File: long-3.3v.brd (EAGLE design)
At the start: 43.8 x 50.2 mm, 20 parts, among them U1 USD-SOCKET, U2 MCP73831, U4 ADXL375BCCZ, X1 Micro USB

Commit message: Added RFM69HW and more stuff
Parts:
- added U$3: RFM69HW, RFM69HW:RFM69HW
- JP1, JP2, JP5, JP6: device pinhead:1X04 -> pinhead:1X02
- moved U$1 7.51 mm to (6.40, 8.30)
- moved JP2 7.50 mm to (18.4, 13.2)
- moved JP1 7.40 mm to (1.70, 13.2)
- moved U1 2.30 mm to (3.00, 34.5)
- moved JP4 0.60 mm to (18.7, 40.2)
- moved JP3 0.50 mm to (1.30, 40.3)
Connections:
- new net N$1: U$1.P$24, U$1.P$36, U$1.P$48
- new net N$2: U$1.P$23, U$1.P$35, U$1.P$47, U$1.P$49
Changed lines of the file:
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@@
 </autorouter>
 <elements>
-<element name="U1" library="SparkFun-Connectors" package="MICROSD_1:1" value="USD-SOCKET" x="3" y="32.2">
-<attribute name="PROD_ID" value="CONN-07820" x="3" y="32.2" size="1.778" layer="27" display="off"/>
+<element name="U1" library="SparkFun-Connectors" package="MICROSD_1:1" value="USD-SOCKET" x="3" y="34.5">
+<attribute name="PROD_ID" value="CONN-07820" x="3" y="34.5" size="1.778" layer="27" display="off"/>
 </element>
 <element name="D11" library="SparkFun" package="LED-0603" value="RED" x="1.4" y="7.4" rot="MR180"/>
@@
 <element name="X1" library="SparkFun" package="USB-MICROB" value="Micro USB" x="10" y="1.5"/>
 <element name="U$2" library="Ava" package="UBLOX_MAX" value="UBLOX_MAX" x="33.3" y="26.5"/>
-<element name="JP1" library="pinhead" package="1X04" value="" x="1.7" y="20.6" rot="MR90"/>
-<element name="JP2" library="pinhead" package="1X04" value="" x="18.4" y="20.7" rot="MR90"/>
-<element name="JP3" library="pinhead" package="1X04" value="" x="1.3" y="39.8" rot="MR90"/>
-<element name="JP4" library="pinhead" package="1X04" value="" x="18.7" y="39.6" rot="MR90"/>
-<element name="JP5" library="pinhead" package="1X04" value="" x="25.5" y="20.7" rot="MR90"/>
-<element name="JP6" library="pinhead" package="1X04" value="" x="42.2" y="20.7" rot="MR90"/>
+<element name="JP1" library="pinhead" package="1X02" value="" x="1.7" y="13.2" rot="MR90"/>
+<element name="JP2" library="pinhead" package="1X02" value="" x="18.4" y="13.2" rot="MR90"/>
+<element name="JP3" library="pinhead" package="1X04" value="" x="1.3" y="40.3" rot="MR90"/>
+<element name="JP4" library="pinhead" package="1X04" value="" x="18.7" y="40.2" rot="MR90"/>
+<element name="JP5" library="pinhead" package="1X02" value="" x="25.5" y="20.7" rot="MR90"/>
+<element name="JP6" library="pinhead" package="1X02" value="" x="42.2" y="20.7" rot="MR90"/>
 <element name="JP8" library="pinhead" package="1X04" value="" x="25.2" y="39.5" rot="MR90"/>
 <element name="JP9" library="pinhead" package="1X04" value="" x="42.4" y="39.6" rot="MR90"/>
 <element name="U4" library="adxl375bccz" package="LGA_CC-14-1" value="ADXL375BCCZ" x="33.4" y="42.1"/>
-<element name="U$1" library="STM32F411CEU6" package="STM32F411CEU6" value="STM32F411CEU6" x="6.7" y="15.8"/>
+<element name="U$1" library="STM32F411CEU6" package="STM32F411CEU6" value="STM32F411CEU6" x="6.4" y="8.3"/>
+<element name="U$3" library="RFM69HW" package="RFM69HW" value="RFM69HW" x="9.8" y="25.5" rot="R180"/>
 </elements>
 <signals>
@@
 <wire x1="10.25" y1="5.65" x2="11" y2="4.9" width="0.2" layer="16"/>
 <wire x1="11" y1="4.9" x2="11" y2="2.8" width="0.2" layer="16"/>
-<wire x1="11" y1="4.9" x2="11.3" y2="4.15" width="0" layer="19" extent="1-16"/>
 <wire x1="3" y1="6.85" x2="3.5" y2="6.85" width="0.2" layer="16"/>
 <wire x1="3.5" y1="6.85" x2="4.7" y2="5.65" width="0.2" layer="16"/>
@@
 <wire x1="3" y1="6.85" x2="2.4" y2="6.25" width="0.2" layer="16"/>
 <wire x1="2.4" y1="6.25" x2="2.4" y2="5.3001" width="0.2" layer="16"/>
+<wire x1="11" y1="4.9" x2="11.3" y2="4.15" width="0" layer="19" extent="1-16"/>
 </signal>
 <signal name="VBAT">
@@
 <contactref element="U$2" pad="1_GND"/>
 </signal>
+<signal name="N$1">
+<contactref element="U$1" pad="P$24"/>
+<contactref element="U$1" pad="P$48"/>
+<contactref element="U$1" pad="P$36"/>
+<wire x1="12.65" y1="8.525" x2="13.175" y2="14.55" width="0" layer="19" extent="1-1"/>
+<wire x1="7.15" y1="15.075" x2="13.175" y2="14.55" width="0" layer="19" extent="1-1"/>
+</signal>
+<signal name="N$2">
+<contactref element="U$1" pad="P$23"/>
+<contactref element="U$1" pad="P$35"/>
+<contactref element="U$1" pad="P$47"/>
+<contactref element="U$1" pad="P$49"/>
+<wire x1="9.9" y1="11.8" x2="13.175" y2="14.05" width="0" layer="19" extent="1-1"/>
+<wire x1="7.65" y1="15.075" x2="9.9" y2="11.8" width="0" layer="19" extent="1-1"/>
+<wire x1="12.15" y1="8.525" x2="9.9" y2="11.8" width="0" layer="19" extent="1-1"/>
+</signal>
 </signals>

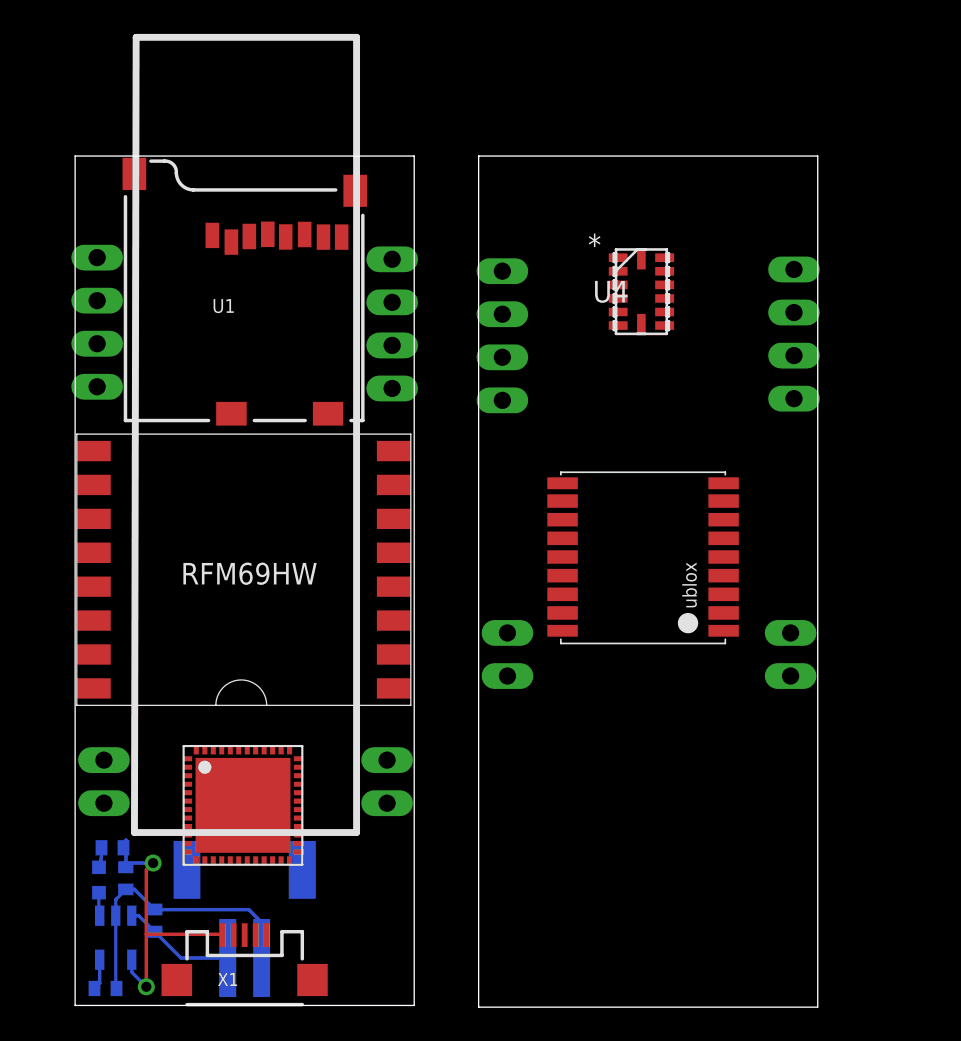
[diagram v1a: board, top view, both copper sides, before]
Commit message: Updated schematic, connected peripherals
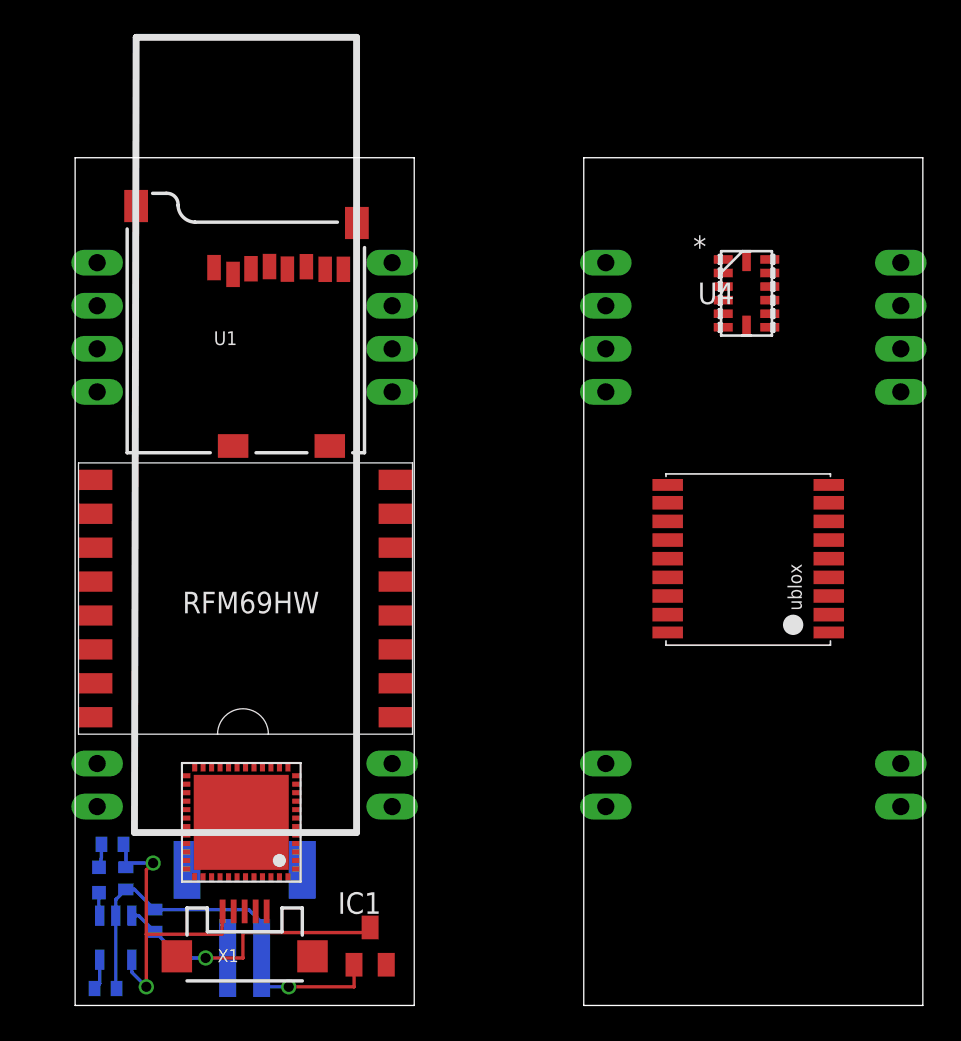
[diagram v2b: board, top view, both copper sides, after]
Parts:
- added IC1: (no value), v-reg:SOT23
- moved JP6 10.1 mm to (48.7, 13.0)
- moved JP5 9.64 mm to (31.3, 13.0)
- moved U$1 9.14 mm to (13.3, 14.3), turned to 180 degrees
- moved JP9 6.31 mm to (48.7, 40.0)
- moved U$2 6.20 mm to (39.5, 26.4)
- moved U4 6.20 mm to (39.6, 42.0)
- moved JP8 6.12 mm to (31.3, 40.0)
- moved U1 1.90 mm to (3.10, 32.6)
- moved U$3 1.70 mm to (9.90, 23.8)
- moved X1 1.40 mm to (10.0, 2.90)
- moved JP1 0.45 mm to (1.30, 13.0)
- moved JP2 0.36 mm to (18.7, 13.0)
- moved JP3 0.30 mm to (1.30, 40.0)
- moved JP4 0.20 mm to (18.7, 40.0)
- moved R3 0.20 mm to (2.20, 9.50)
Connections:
- removed net 10_GND: U$2.10_GND
- removed net 12_GND: U$2.12_GND
- removed net 1_GND: U$2.1_GND
- removed net 7_VCC_IO: U$2.7_VCC_IO
- removed net 8_VCC: U$2.8_VCC
- removed net 9_V_RESET: U$2.9_V_RESET
- removed net N$1: U$1.P$24, U$1.P$36, U$1.P$48
- removed net N$2: U$1.P$23, U$1.P$35, U$1.P$47, U$1.P$49
- new net FC_RX: U$1.P$31
- new net FC_TX: U$1.P$30
- new net GPS_RX: U$2.3_RXD1
- new net GPS_TX: U$2.2_TXD1
- new net RADIO_CS: U$1.P$25, U$3.NSS
- new net RADIO_MISO: U$1.P$27, U$3.MISO
- new net RADIO_MOSI: U$1.P$28, U$3.MOSI
- new net RADIO_SCK: U$1.P$26, U$3.SCK
- new net SCL: U$1.P$42, U4.14
- new net SDA: U$1.P$43, U4.13
- new net SD_CS: U$1.P$14, U1.2
- new net SD_MISO: U$1.P$16, U1.7
- new net SD_MOSI: U$1.P$17, U1.3
- new net SD_SCK: U$1.P$15, U1.5
- new net VCC: IC1.2, U$1.P$24, U$1.P$36, U$1.P$48, U$2.14_VCC_RF, U$2.6_V_BCKP, U$2.7_VCC_IO, U$2.8_VCC, U$2.9_V_RESET, U$3.3.3V, U1.4, U4.1, U4.6
- net GND: now also IC1.1, U$1.P$23, U$1.P$35, U$1.P$47, U$1.P$49, U$2.10_GND, U$2.12_GND, U$2.1_GND, U$3.GND, U$3.GND_2, U1.6, U1.GND1, U1.GND3, U4.2, U4.4, U4.5
- net VBAT: now also IC1.3
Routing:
- net VBAT: track 6.69 -> 18.2 mm, vias 0 -> 1
- net GND: track 17.0 -> 25.5 mm, vias 0 -> 1
- net VIN: track 17.8 -> 18.9 mm
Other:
- board size 43.8 x 50.2 mm -> 50 x 50 mm

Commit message: Connected USB & Crystal Routed base PCB
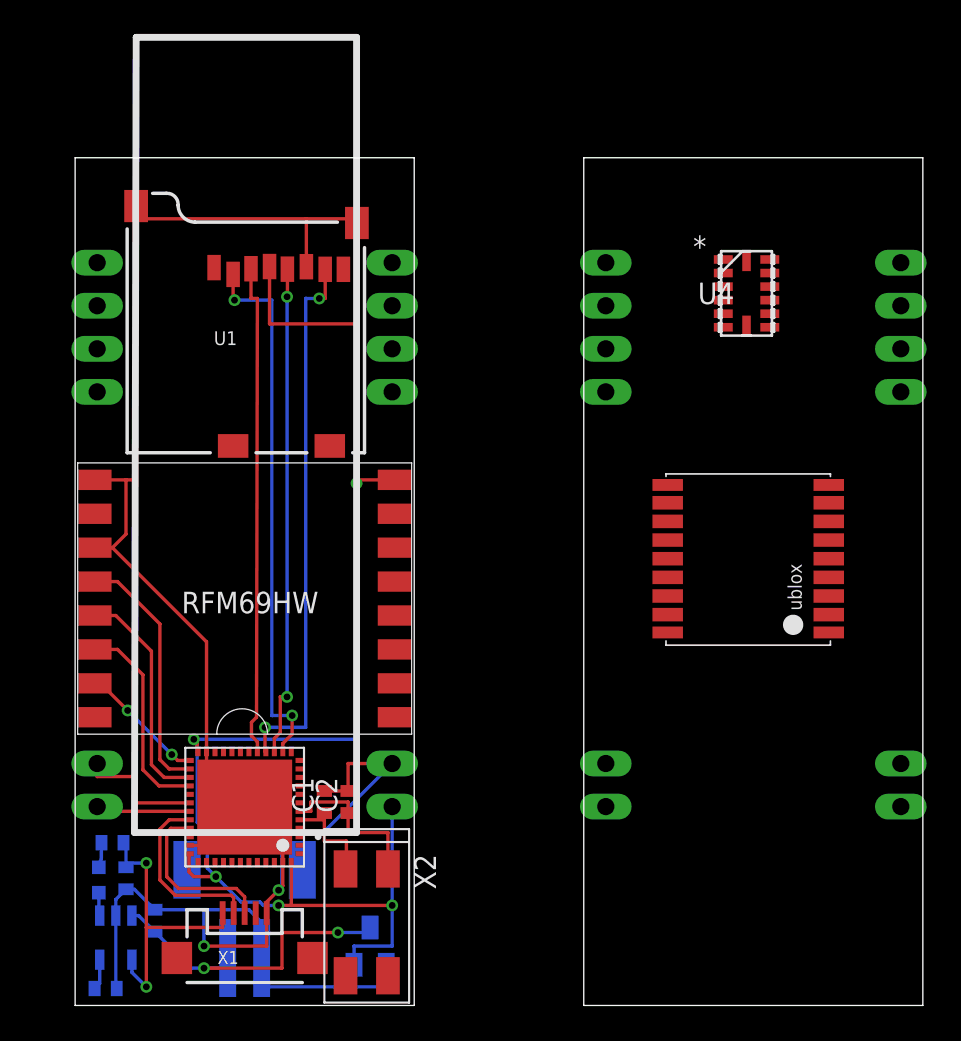
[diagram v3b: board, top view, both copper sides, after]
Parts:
- added C1, C2: 20pF, rcl:C0402
- added X2: CRYSTALS-NOGND-12SMX-B, IQD-Frequency-Products:7.5X5-4-PAD
- moved U$1 0.92 mm to (13.5, 15.2)
- moved X1 0.10 mm to (10.0, 2.80)
- moved R3 0.10 mm to (2.20, 9.60)
- moved U$3 0.05 mm to (9.85, 23.8)
- flipped IC1 to the bottom
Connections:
- new net N$1: C1.1, U$1.P$5, X2.1
- new net N$2: C2.1, U$1.P$6, X2.4
- new net USB_D+: U$1.P$33, X1.D+
- new net USB_D-: U$1.P$32, X1.D-
- net FC_RX: now also JP1.1
- net FC_TX: now also JP1.2
- net GND: now also C1.2, C2.2, JP2.2, JP6.2
- net GPS_RX: now also JP5.2
- net GPS_TX: now also JP5.1
- net VCC: now also JP2.1, JP6.1
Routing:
- net GND: track 25.5 -> 127.4 mm, vias 1 -> 2
- net VCC: track 0.00 -> 82.6 mm, vias 0 -> 5
- net SD_MISO: track 0.00 -> 32.0 mm, vias 0 -> 2
- net SD_CS: track 0.00 -> 31.9 mm, vias 0 -> 2
- net SD_MOSI: track 0.00 -> 29.1 mm
- net SD_SCK: track 0.00 -> 29.0 mm, vias 0 -> 2
- net RADIO_SCK: track 0.00 -> 14.8 mm
- net RADIO_MISO: track 0.00 -> 13.5 mm
- net RADIO_MOSI: track 0.00 -> 12.2 mm
- net USB_D-: track 0.00 -> 10.6 mm
- net USB_D+: track 0.00 -> 10.1 mm
- net N$2: track 0.00 -> 9.67 mm
- net FC_TX: track 0.00 -> 7.75 mm
- net RADIO_CS: track 0.00 -> 7.46 mm, vias 0 -> 2
- net N$1: track 0.00 -> 6.07 mm
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
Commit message: Added Components Added decoupling capacitors Changed pin headers to round pads
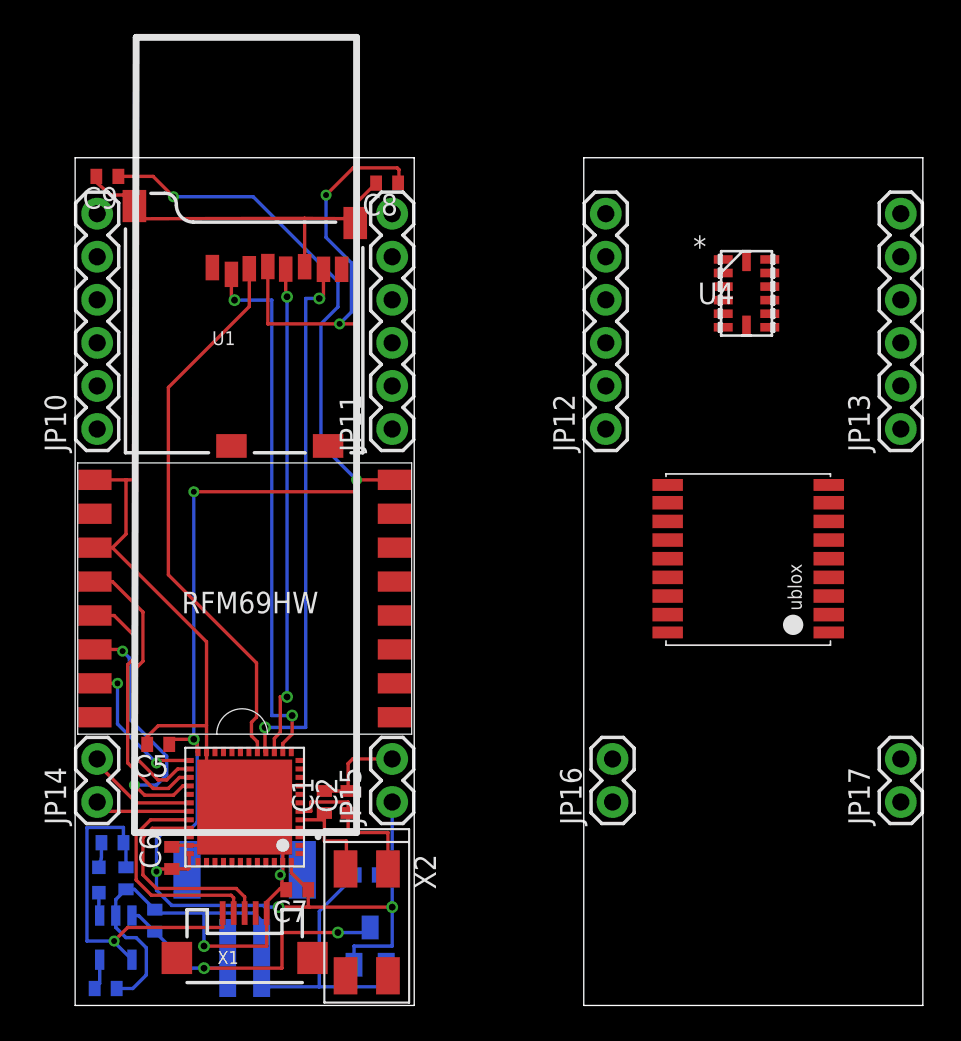
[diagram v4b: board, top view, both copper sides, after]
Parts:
- removed JP1, JP2, JP5, JP6: (no value), pinhead:1X02
- removed JP3, JP4, JP8, JP9: (no value), pinhead:1X04
- added C10: 1uF, rcl:C0402
- added C5, C6, C7, C8, C9: 100nF, rcl:C0402
- added JP10, JP11, JP12, JP13: (no value), SparkFun-Connectors:1X06
- added JP14, JP15, JP16, JP17: M02PTH, SparkFun-Connectors:1X02
- moved U1 0.10 mm to (3.00, 32.6)
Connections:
- net FC_RX: now also JP14.1; no longer JP1.1
- net FC_TX: now also JP14.2; no longer JP1.2
- net GND: now also C10.2, C5.2, C6.2, C7.2, C8.2, C9.2, JP15.2, JP17.2; no longer JP2.2, JP6.2
- net GPS_RX: now also JP16.2; no longer JP5.2
- net GPS_TX: now also JP16.1; no longer JP5.1
- net VCC: now also C10.1, C5.1, C6.1, C7.1, C8.1, C9.1, JP15.1, JP17.1; no longer JP2.1, JP6.1
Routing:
- net VCC: track 82.6 -> 134.1 mm, vias 5 -> 9
- net GND: track 127.4 -> 142.5 mm
- net VIN: track 17.8 -> 22.5 mm, vias 2 -> 1
- net SD_MOSI: track 29.1 -> 32.9 mm
- net RADIO_MOSI: track 12.2 -> 15.9 mm, vias 0 -> 2
- net USB_D-: track 10.6 -> 13.3 mm
- net USB_D+: track 10.1 -> 12.6 mm
- net RADIO_MISO: track 13.5 -> 15.0 mm
- net RADIO_SCK: track 14.8 -> 16.4 mm
- net RADIO_CS: track 7.46 -> 8.99 mm
- net FC_TX: track 7.75 -> 6.66 mm

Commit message: Added more parts, routed more lines Added UFL connector (unrouted) Added and routed pullups, programming header, and other stuff
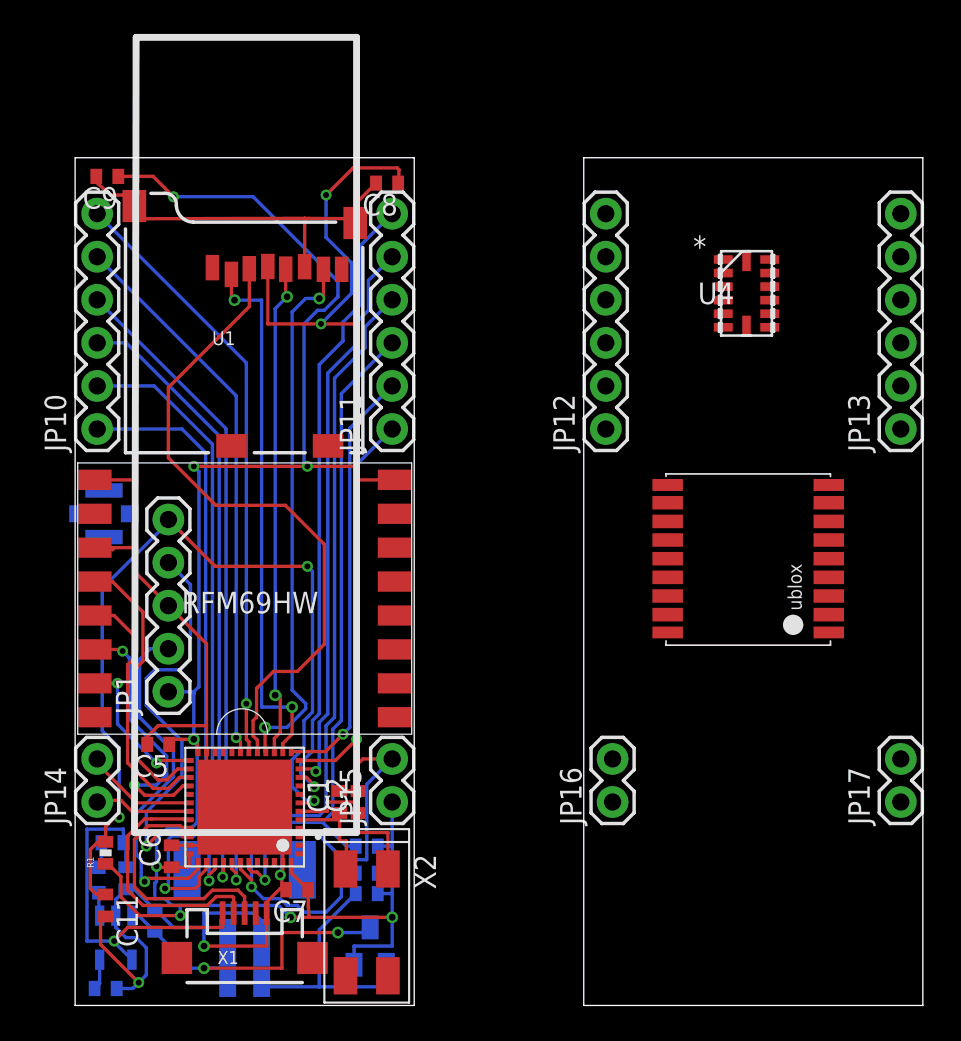
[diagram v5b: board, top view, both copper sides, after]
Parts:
- added C11: 100nF, rcl:C0402
- added JP1: (no value), SparkFun:1X05
- added R1: 10k, SparkFun:0402-RES
- added R2, R5: 3k3, SparkFun:0402-RES
- added U$4: U.FL, SparkFun:U.FL
- moved C10 1.10 mm to (17.2, 6.60)
- moved C1 0.90 mm to (15.6, 12.0)
- moved C2 0.60 mm to (16.7, 12.0)
- moved C6 0.10 mm to (5.67, 8.80)
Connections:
- new net N$4: U$3.ANT, U$4.P$3
- new net NRST: C11.1, JP1.5, R1.2, U$1.P$7
- new net PA0: JP11.6, U$1.P$10
- new net PA1: JP11.5, U$1.P$11
- new net PB0: JP10.6, U$1.P$18
- new net PB1: JP10.5, U$1.P$19
- new net RX: JP11.2, U$1.P$13
- new net SPI_CS: JP10.1, U$1.P$38
- new net SPI_MISO: JP10.3, U$1.P$40
- new net SPI_MOSI: JP10.4, U$1.P$41
- new net SPI_SCK: JP10.2, U$1.P$39
- new net SWCLK: JP1.2, U$1.P$37
- new net SWDIO: JP1.4, U$1.P$34
- new net TX: JP11.1, U$1.P$12
- net GND: now also C11.2, JP1.3, U$4.P$1, U$4.P$2
- net SCL: now also JP11.4, R2.2
- net SDA: now also JP11.3, R5.2
- net VCC: now also JP1.1, R1.1, R2.1, R5.1
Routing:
- net NRST: track 0.00 -> 51.4 mm, vias 0 -> 3
- net SCL: track 0.00 -> 49.4 mm, vias 0 -> 1
- net SDA: track 0.00 -> 40.2 mm, vias 0 -> 1
- net SPI_MOSI: track 0.00 -> 38.8 mm, vias 0 -> 1
- net SPI_CS: track 0.00 -> 38.0 mm, vias 0 -> 1
- net PA0: track 0.00 -> 37.5 mm, vias 0 -> 1
- net SPI_MISO: track 0.00 -> 36.4 mm, vias 0 -> 1
- net PB0: track 0.00 -> 35.4 mm, vias 0 -> 1
- net SPI_SCK: track 0.00 -> 35.3 mm, vias 0 -> 1
- net PA1: track 0.00 -> 33.2 mm, vias 0 -> 1
- net PB1: track 0.00 -> 32.7 mm, vias 0 -> 1
- net RX: track 0.00 -> 25.2 mm, vias 0 -> 1
- net SWDIO: track 0.00 -> 23.9 mm, vias 0 -> 1
- net TX: track 0.00 -> 23.0 mm, vias 0 -> 1
- net SWCLK: track 0.00 -> 20.8 mm, vias 0 -> 1
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
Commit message: fixed headers
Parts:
- X2: value CRYSTALS-NOGND-12SMX-B -> CRYSTAL
- moved U4 17.2 mm to (40.5, 24.8)
- moved U$2 12.8 mm to (40.4, 13.6), turned to 270 degrees
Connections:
- net FC_RX: now also JP16.1; no longer JP14.1
- net FC_TX: now also JP16.2; no longer JP14.2
- net GPS_RX: now also JP14.2; no longer JP16.2
- net GPS_TX: now also JP14.1; no longer JP16.1
- net PA0: now also JP12.6
- net PA1: now also JP12.5
- net PB0: now also JP13.6
- net PB1: now also JP13.5
- net RX: now also JP12.2
- net SCL: now also JP12.4
- net SDA: now also JP12.3
- net SPI_CS: now also JP13.1
- net SPI_MISO: now also JP13.3
- net SPI_MOSI: now also JP13.4
- net SPI_SCK: now also JP13.2
- net TX: now also JP12.1
